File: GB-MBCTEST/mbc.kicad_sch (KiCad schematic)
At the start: 8 parts

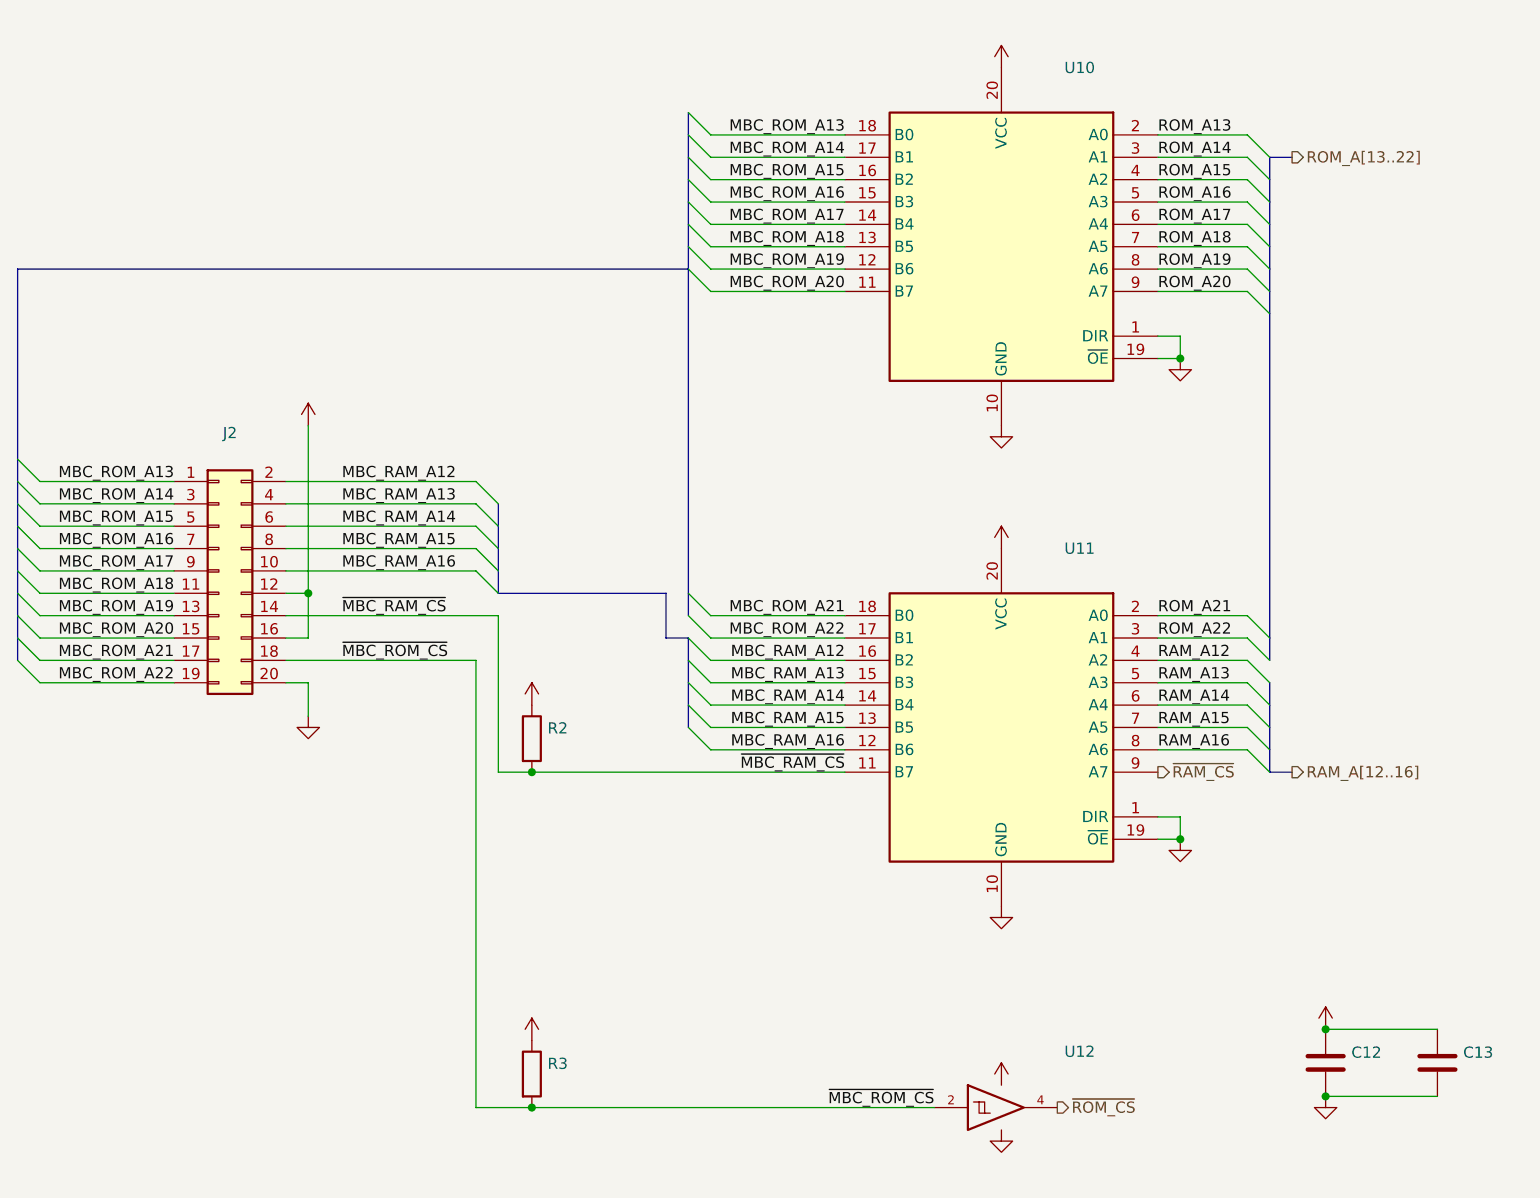
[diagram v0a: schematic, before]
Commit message: Upgrade projects to KiCad 7
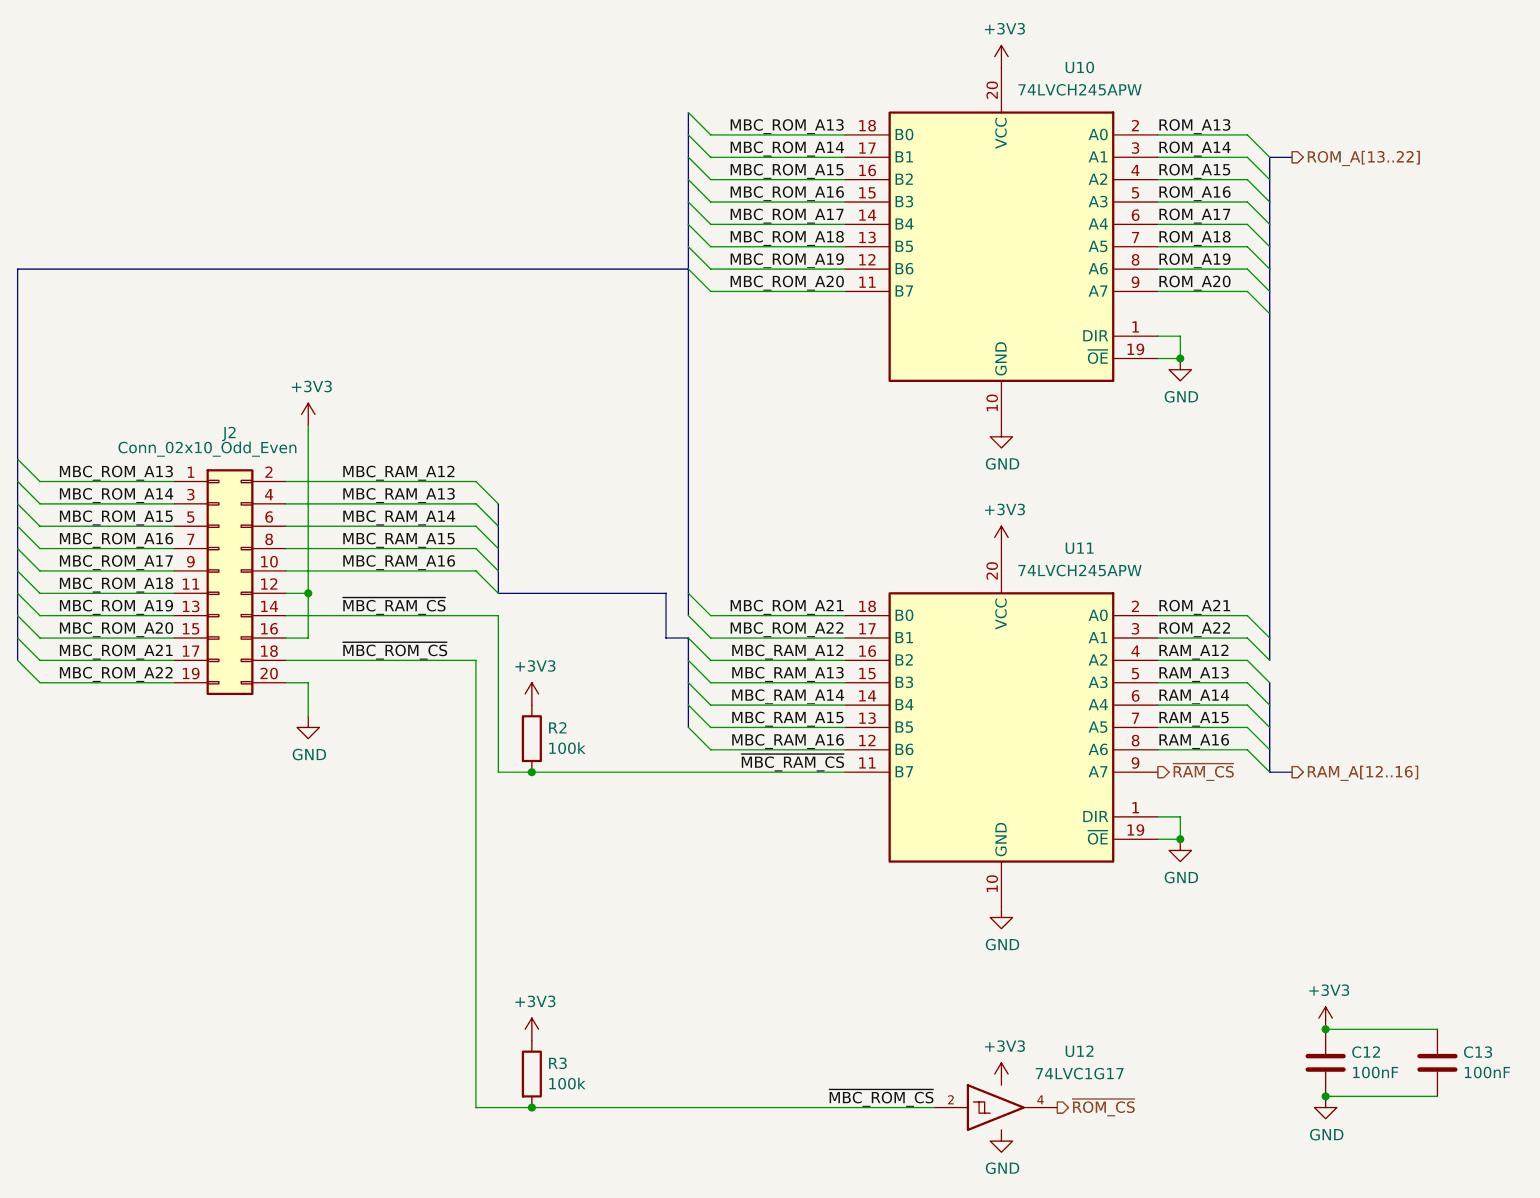
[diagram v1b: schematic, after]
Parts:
- C12, C13: value (none) -> 100nF; footprint (none) -> Capacitor_SMD:C_0603_1608Metric
- J2: value (none) -> Conn_02x10_Odd_Even; footprint (none) -> Connector_PinHeader_2.54mm:PinHeader_2x10_P2.54mm_Vertical_SMD
- R2, R3: value (none) -> 100k; footprint (none) -> Resistor_SMD:R_0603_1608Metric
- U10, U11: value (none) -> 74LVCH245APW; footprint (none) -> Package_SO:TSSOP-20_4.4x6.5mm_P0.65mm
- U12: value (none) -> 74LVC1G17; footprint (none) -> Package_TO_SOT_SMD:SOT-353_SC-70-5
